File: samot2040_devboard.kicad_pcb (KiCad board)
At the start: 2 copper layers, 4 parts, among them J1 USB_C_Receptacle_USB2.0_16P, U1 RP2040, U2 MCP1700x-330xxTT, U3 W25Q128JVS

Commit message: upload
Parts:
- added C1: 1uF, Capacitor_SMD:C_0402_1005Metric_Pad0.74x0.62mm_HandSolder, F.Cu at (166.2, 60.9)
- added C10: 1uF, Capacitor_SMD:C_0402_1005Metric_Pad0.74x0.62mm_HandSolder, F.Cu at (163.6, 71.2)
- added C11: 0.1uF, Capacitor_SMD:C_0402_1005Metric_Pad0.74x0.62mm_HandSolder, F.Cu at (162.3, 82.0)
- added C12: 0.1uF, Capacitor_SMD:C_0402_1005Metric_Pad0.74x0.62mm_HandSolder, F.Cu at (159.8, 70.3)
- added C13: 10uF, Capacitor_SMD:C_0603_1608Metric_Pad1.08x0.95mm_HandSolder, F.Cu at (166.1, 59.6)
- added C14: 10uF, Capacitor_SMD:C_0603_1608Metric_Pad1.08x0.95mm_HandSolder, F.Cu at (163.7, 54.8)
- added C15: 30pF, Capacitor_SMD:C_0603_1608Metric_Pad1.08x0.95mm_HandSolder, F.Cu at (164.7, 85.0)
- added C16: 30pF, Capacitor_SMD:C_0603_1608Metric_Pad1.08x0.95mm_HandSolder, F.Cu at (157.6, 85.5)
- added C17: 0.1uF, Capacitor_SMD:C_0402_1005Metric_Pad0.74x0.62mm_HandSolder, F.Cu at (161.7, 68.3)
- added C18: 0.1uF, Capacitor_SMD:C_0402_1005Metric_Pad0.74x0.62mm_HandSolder, F.Cu at (164.7, 82.2)
- added C2: 0.1uF, Capacitor_SMD:C_0402_1005Metric_Pad0.74x0.62mm_HandSolder, F.Cu at (164.5, 71.2)
- added C3: 0.1uF, Capacitor_SMD:C_0402_1005Metric_Pad0.74x0.62mm_HandSolder, F.Cu at (166.1, 72.7)
- added C4: 0.1uF, Capacitor_SMD:C_0402_1005Metric_Pad0.74x0.62mm_HandSolder, F.Cu at (156.4, 73.0)
- added C5: 0.1uF, Capacitor_SMD:C_0402_1005Metric_Pad0.74x0.62mm_HandSolder, F.Cu at (160.7, 68.3)
- added C6: 0.1uF, Capacitor_SMD:C_0402_1005Metric_Pad0.74x0.62mm_HandSolder, F.Cu at (155.4, 78.0)
- added C7: 0.1uF, Capacitor_SMD:C_0402_1005Metric_Pad0.74x0.62mm_HandSolder, F.Cu at (166.2, 77.9)
- added C8: 0.1uF, Capacitor_SMD:C_0402_1005Metric_Pad0.74x0.62mm_HandSolder, F.Cu at (166.1, 73.6)
- added C9: 0.1uF, Capacitor_SMD:C_0402_1005Metric_Pad0.74x0.62mm_HandSolder, F.Cu at (162.6, 83.0)
- added J2: Conn_01x20, Connector_PinHeader_2.54mm:PinHeader_1x20_P2.54mm_Vertical, B.Cu at (151.8, 48.1)
- added J3: Conn_01x20, Connector_PinHeader_2.54mm:PinHeader_1x20_P2.54mm_Vertical, B.Cu at (169.6, 48.1)
- added R1: 5.1K, Resistor_SMD:R_0603_1608Metric_Pad0.98x0.95mm_HandSolder, F.Cu at (157.6, 55.9)
- added R2: 5.1K, Resistor_SMD:R_0603_1608Metric_Pad0.98x0.95mm_HandSolder, F.Cu at (156.1, 55.9)
- added R3: 27, Resistor_SMD:R_0402_1005Metric_Pad0.72x0.64mm_HandSolder, F.Cu at (162.6, 71.1)
- added R4: 27, Resistor_SMD:R_0402_1005Metric_Pad0.72x0.64mm_HandSolder, F.Cu at (161.7, 71.1)
- added R5: 1k, Resistor_SMD:R_0603_1608Metric_Pad0.98x0.95mm_HandSolder, F.Cu at (159.2, 82.5)
- added R6: 1k, Resistor_SMD:R_0603_1608Metric_Pad0.98x0.95mm_HandSolder, F.Cu at (155.1, 83.6)
- added R7: 10k, Resistor_SMD:R_0603_1608Metric_Pad0.98x0.95mm_HandSolder, F.Cu at (155.1, 80.2)
- added R9: 10k, Resistor_SMD:R_0603_1608Metric_Pad0.98x0.95mm_HandSolder, F.Cu at (166.7, 86.8)
- added SW1: SW_Push, Button_Switch_SMD:SW_SPST_B3U-1000P-B, F.Cu at (156.9, 91.0)
- added SW2: SW_Push, Button_Switch_SMD:SW_SPST_B3U-1000P-B, F.Cu at (164.6, 91.0)
- added Y1: 12 MHz, Crystal:Crystal_SMD_3225-4Pin_3.2x2.5mm_HandSoldering, F.Cu at (161.1, 85.8)
- U3: value W25Q128JVS -> MX25L6433FM2I-08G
- moved J1 78.6 mm to (163.6, 52.9), turned to 180 degrees
- moved U3 77.0 mm to (160.7, 64.0)
- moved U2 70.6 mm to (166.1, 56.9), turned to 90 degrees
- moved U1 61.6 mm to (160.8, 77.0)
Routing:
- net +3V3: track 0.00 -> 82.5 mm
- net GND: track 0.00 -> 73.6 mm, vias 0 -> 13
- net GPIO0: track 0.00 -> 31.0 mm
- net GPIO1: track 0.00 -> 28.3 mm
- net QSPI_SS: track 0.00 -> 26.1 mm, vias 0 -> 2
- net GPIO2: track 0.00 -> 24.4 mm
- net USB_D-: track 0.00 -> 24.1 mm, vias 0 -> 1
- net GPIO15: track 0.00 -> 23.2 mm, vias 0 -> 1
- net USB_D+: track 0.00 -> 22.5 mm, vias 0 -> 1
- net VBUS: track 0.00 -> 21.8 mm
- net GPIO3: track 0.00 -> 21.6 mm
- net GPIO16: track 0.00 -> 21.2 mm, vias 0 -> 1
- net GPIO4: track 0.00 -> 19.6 mm
- net GPIO14: track 0.00 -> 19.3 mm, vias 0 -> 1
- net +1V1: track 0.00 -> 19.3 mm, vias 0 -> 3
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- added copper zone on B.Cu, net GND
- added copper zone on F.Cu, net GND
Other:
- board outline added: 21 x 51 mm
- board text added: "BOOT"
- board text added: "Reset"
- board text added: "SamotPI2040"

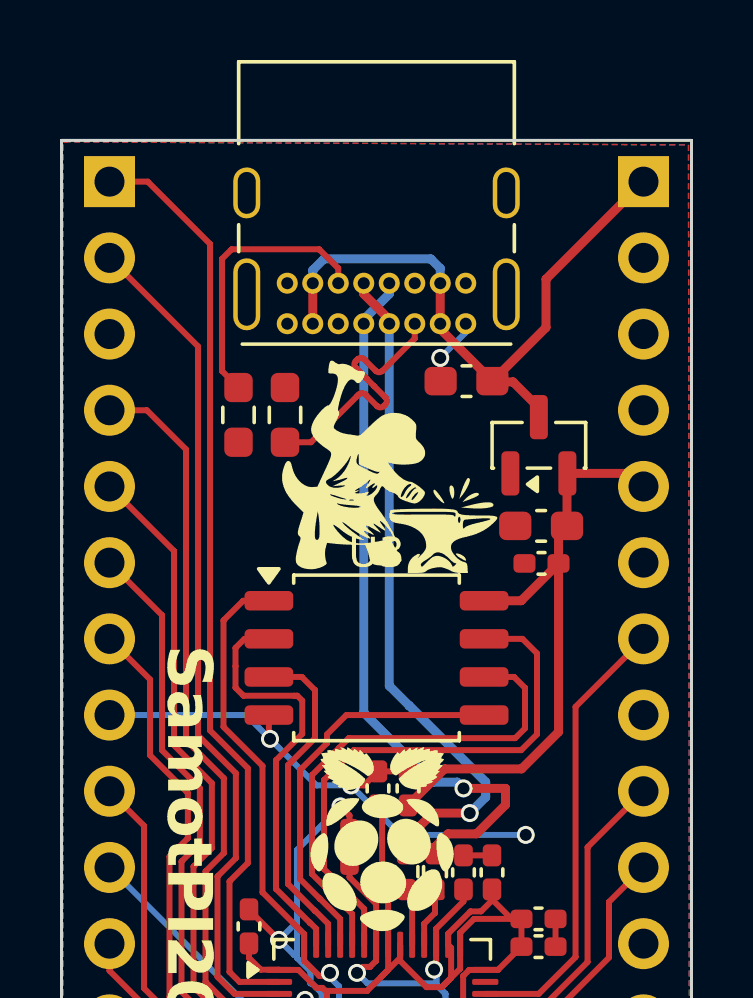
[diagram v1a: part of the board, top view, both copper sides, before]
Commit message: Update USB-C connector
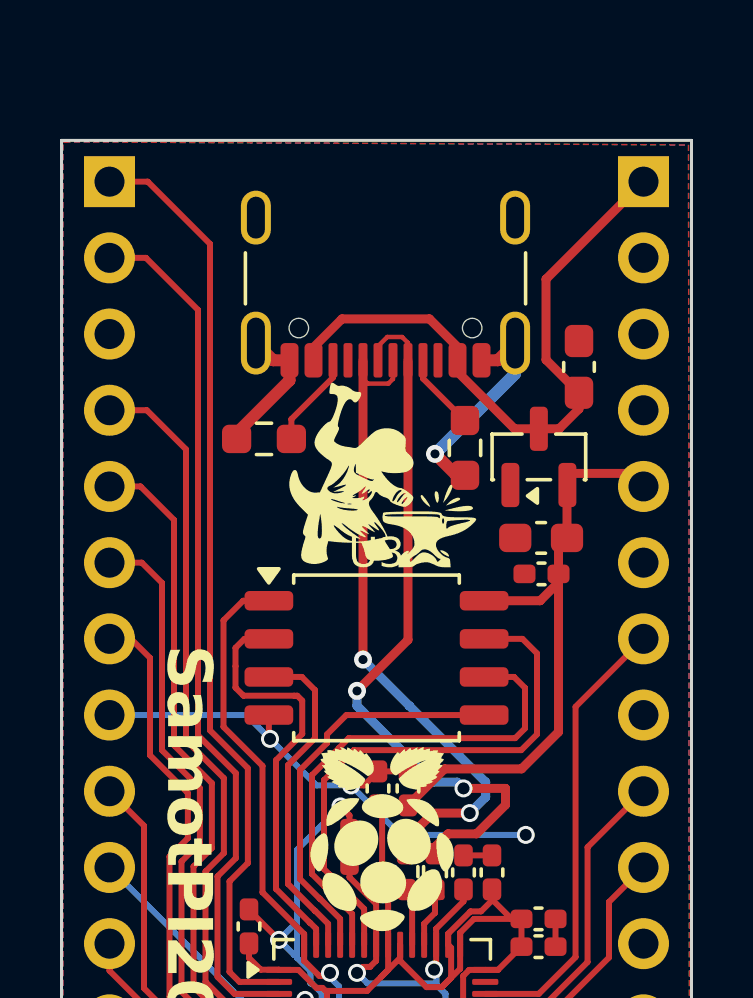
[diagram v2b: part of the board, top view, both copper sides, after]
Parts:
- J1: footprint Connector_USB:USB_C_Receptacle_GCT_USB4085 -> Connector_USB:USB_C_Receptacle_GCT_USB4105-xx-A_16P_TopMnt_Horizontal
- moved R1 6.10 mm to (163.6, 57.0), turned to -90 degrees
- moved C14 3.78 mm to (167.4, 54.3), turned to 90 degrees
- moved J1 3.63 mm to (160.9, 50.4)
- moved R2 1.17 mm to (156.9, 56.7), turned to 180 degrees
- moved C13 0.40 mm to (166.1, 60.0)
- moved U2 0.39 mm to (166.1, 57.3)
- moved C1 0.35 mm to (166.2, 61.2)
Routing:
- net GND: track 73.6 -> 83.5 mm
- net Net-(J1-CC1): track 9.24 -> 2.59 mm
- net Net-(J1-CC2): track 9.28 -> 3.19 mm
- net GPIO1: track 28.3 -> 29.0 mm
- net GPIO4: track 19.6 -> 20.2 mm
- net GPIO3: track 21.6 -> 22.2 mm
- net USB_D-: track 24.1 -> 24.6 mm, vias 1 -> 2
- net USB_D+: track 22.5 -> 22.3 mm, vias 1 -> 2

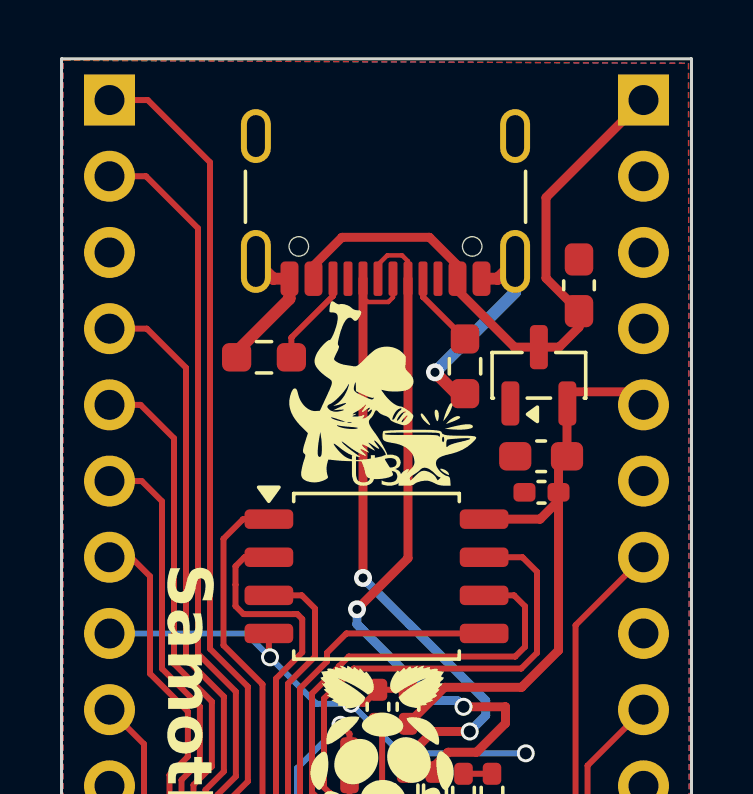
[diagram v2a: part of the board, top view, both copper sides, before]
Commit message: added battery support and charging
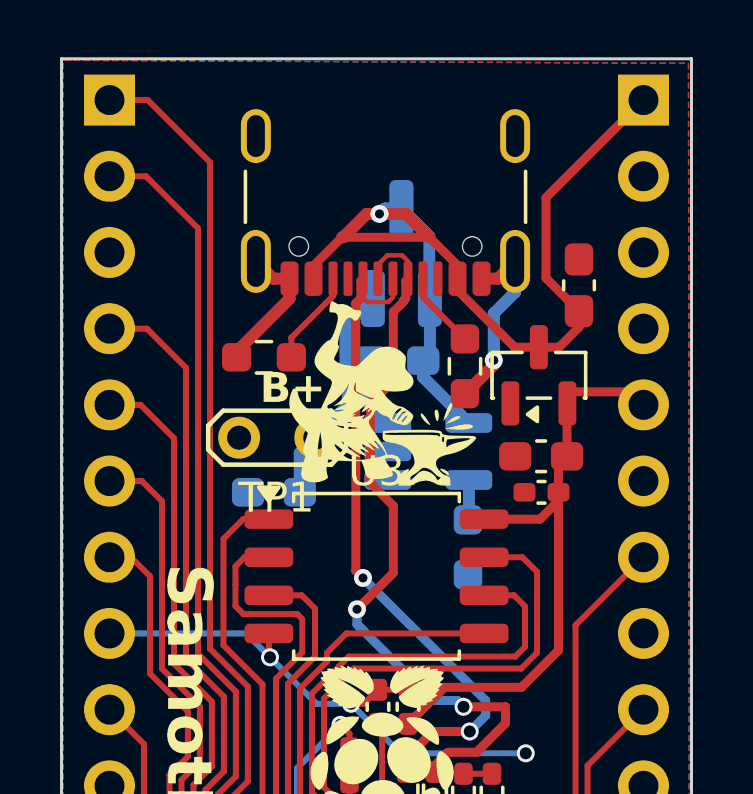
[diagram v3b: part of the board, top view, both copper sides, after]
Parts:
- added C19: 10uF, Capacitor_SMD:C_0603_1608Metric_Pad1.08x0.95mm_HandSolder, B.Cu at (161.3, 56.8)
- added C20: 10uF, Capacitor_SMD:C_0603_1608Metric_Pad1.08x0.95mm_HandSolder, B.Cu at (157.2, 61.2)
- added D1: BAT54C, Package_TO_SOT_SMD:SOT-23_Handsoldering, B.Cu at (161.5, 53.2)
- added R8: 10k, Resistor_SMD:R_0603_1608Metric_Pad0.98x0.95mm_HandSolder, B.Cu at (163.7, 63.0)
- added TP1: TestPoint_2Pole, TestPoint:TestPoint_2Pads_Pitch2.54mm_Drill0.8mm, F.Cu at (158.6, 59.4)
- added U4: MCP73831-2-OT, Package_TO_SOT_SMD:SOT-23-5_HandSoldering, B.Cu at (162.4, 59.8)
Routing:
- net VBUS: track 21.3 -> 34.0 mm, vias 0 -> 1
- net +BATT: track 0.00 -> 9.42 mm
- net Net-(U4-PROG): track 0.00 -> 1.34 mm
- net GND: track 83.5 -> 82.5 mm
- net USB_D-: track 24.6 -> 25.2 mm
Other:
- board text added: "B+"
